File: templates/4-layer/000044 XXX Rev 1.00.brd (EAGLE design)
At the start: 259 x 228 mm, 22 parts, among them X1 PAD_TEST_GROUND_HOOK

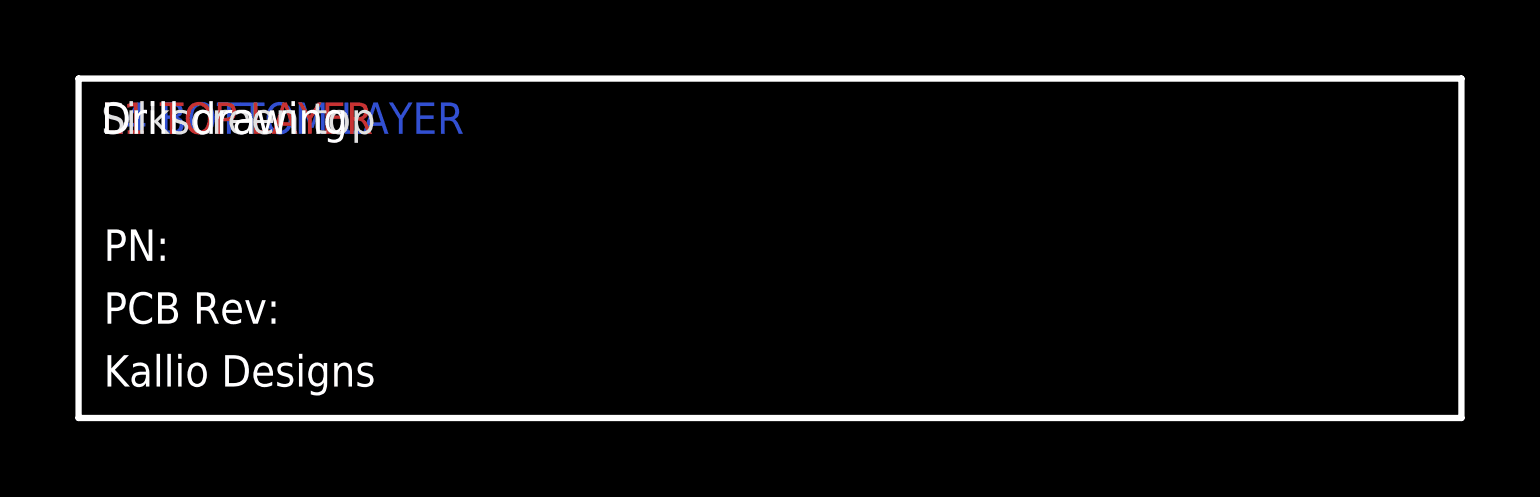
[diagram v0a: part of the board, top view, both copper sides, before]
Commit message: Template updates
For syncing with fusion
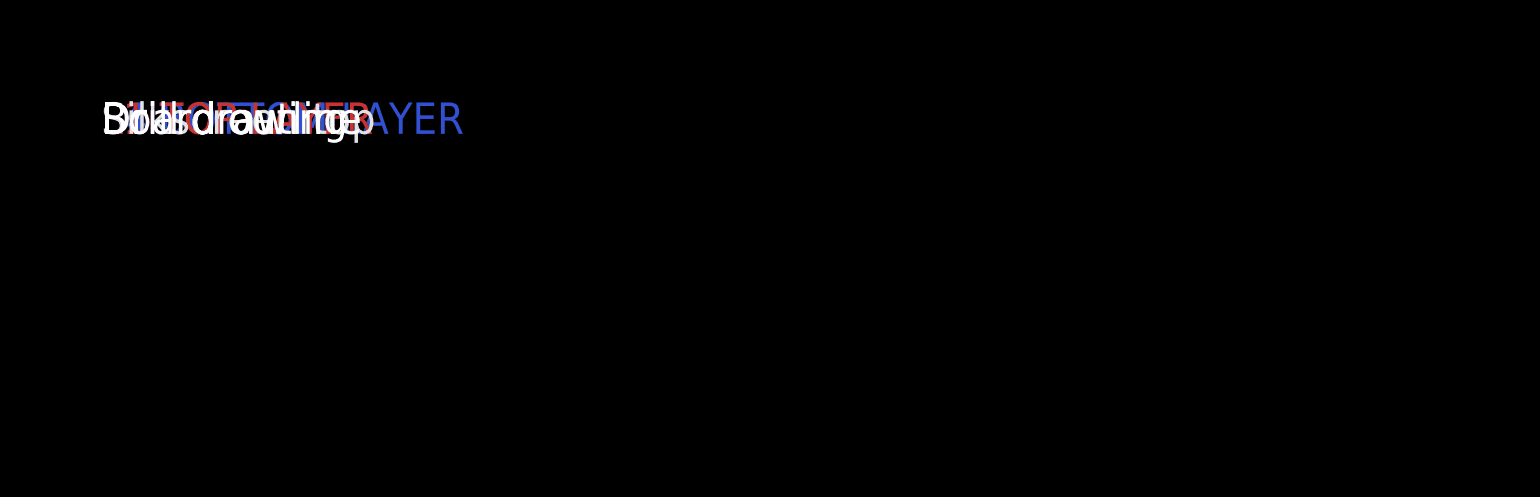
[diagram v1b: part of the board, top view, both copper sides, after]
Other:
- outline, holes or cut-outs redrawn
- board text added: "Board outline"
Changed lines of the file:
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@@
 <layer number="25" name="tNames" color="7" fill="1" visible="yes" active="yes"/>
 <layer number="26" name="bNames" color="11" fill="1" visible="yes" active="yes"/>
-<layer number="27" name="tValues" color="7" fill="1" visible="yes" active="yes"/>
+<layer number="27" name="tValues" color="7" fill="1" visible="no" active="yes"/>
 <layer number="28" name="bValues" color="7" fill="1" visible="no" active="yes"/>
 <layer number="29" name="tStop" color="7" fill="3" visible="yes" active="yes"/>
@@
 <text x="164" y="108" size="2.5" layer="46" font="vector" ratio="12" align="top-right">L3: Mid</text>
 <text x="133" y="27" size="2.5" layer="15" font="vector" ratio="12" align="top-left">L3 mid-layer</text>
-<text x="133.2" y="11.9" size="2.5" layer="20" font="vector" ratio="12" align="top-left">PCB Rev: </text>
+<text x="133.2" y="11.9" size="2.5" layer="48" font="vector" ratio="12" align="top-left">PCB Rev: </text>
 <text x="133" y="27" size="2.5" layer="16" font="vector" ratio="12" align="top-left">L4 BOTTOM LAYER</text>
 <text x="133" y="27" size="2.5" layer="21" font="vector" ratio="12" align="top-left">Silkscreen top</text>
@@
 <text x="133.2" y="23.9" size="2.5" layer="31" font="vector" ratio="12" align="top-left">Paste mask top</text>
 <text x="133.2" y="23.9" size="2.5" layer="32" font="vector" ratio="12" align="top-left">Paste mask bottom</text>
-<wire x1="131.2" y1="28.9" x2="241.2" y2="28.9" width="0.5" layer="20"/>
-<wire x1="241.2" y1="28.9" x2="241.2" y2="1.9" width="0.5" layer="20"/>
-<wire x1="241.2" y1="1.9" x2="131.2" y2="1.9" width="0.5" layer="20"/>
-<wire x1="131.2" y1="1.9" x2="131.2" y2="28.9" width="0.5" layer="20"/>
-<text x="133.2" y="6.9" size="2.5" layer="20" font="vector" ratio="12" align="top-left">&gt;OWNER</text>
-<text x="239.2" y="6.9" size="2.5" layer="20" font="vector" ratio="12" align="top-right">&gt;DATE</text>
-<text x="151.7" y="11.9" size="2.5" layer="20" font="vector" ratio="12" align="top-left">&gt;REVISION</text>
-<text x="133.2" y="16.9" size="2.5" layer="20" font="vector" ratio="12" align="top-left">PN: </text>
-<text x="140.2" y="16.9" size="2.5" layer="20" font="vector" ratio="12" align="top-left">&gt;PCB_PN</text>
+<wire x1="131.2" y1="28.9" x2="241.2" y2="28.9" width="0.5" layer="48"/>
+<wire x1="241.2" y1="28.9" x2="241.2" y2="1.9" width="0.5" layer="48"/>
+<wire x1="241.2" y1="1.9" x2="131.2" y2="1.9" width="0.5" layer="48"/>
+<wire x1="131.2" y1="1.9" x2="131.2" y2="28.9" width="0.5" layer="48"/>
+<text x="133.2" y="6.9" size="2.5" layer="48" font="vector" ratio="12" align="top-left">&gt;OWNER</text>
+<text x="239.2" y="6.9" size="2.5" layer="48" font="vector" ratio="12" align="top-right">&gt;DATE</text>
+<text x="151.7" y="11.9" size="2.5" layer="48" font="vector" ratio="12" align="top-left">&gt;REVISION</text>
+<text x="133.2" y="16.9" size="2.5" layer="48" font="vector" ratio="12" align="top-left">PN: </text>
+<text x="140.2" y="16.9" size="2.5" layer="48" font="vector" ratio="12" align="top-left">&gt;PCB_PN</text>
 <text x="133" y="27" size="2.5" layer="46" font="vector" ratio="12" align="top-left">Drill drawing</text>
 <text x="133" y="27" size="2.5" layer="1" font="vector" ratio="12" align="top-left">L1 TOP LAYER</text>
 <text x="133" y="27" size="2.5" layer="2" font="vector" ratio="12" align="top-left">L2 mid-layer</text>
+<text x="133" y="27" size="2.5" layer="20" font="vector" ratio="12" align="top-left">Board outline</text>
 </plain>
 <attributes>

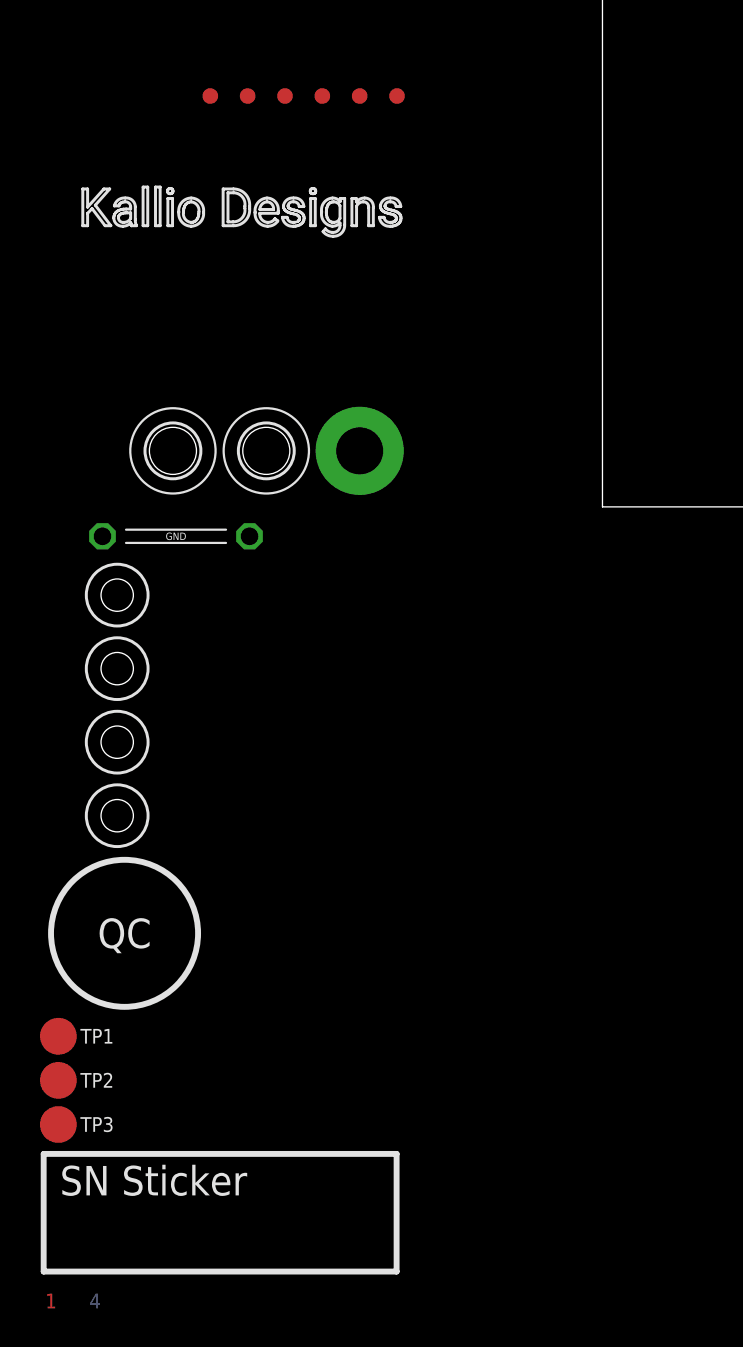
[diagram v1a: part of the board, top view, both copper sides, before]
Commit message: Changed templates to managed libraries
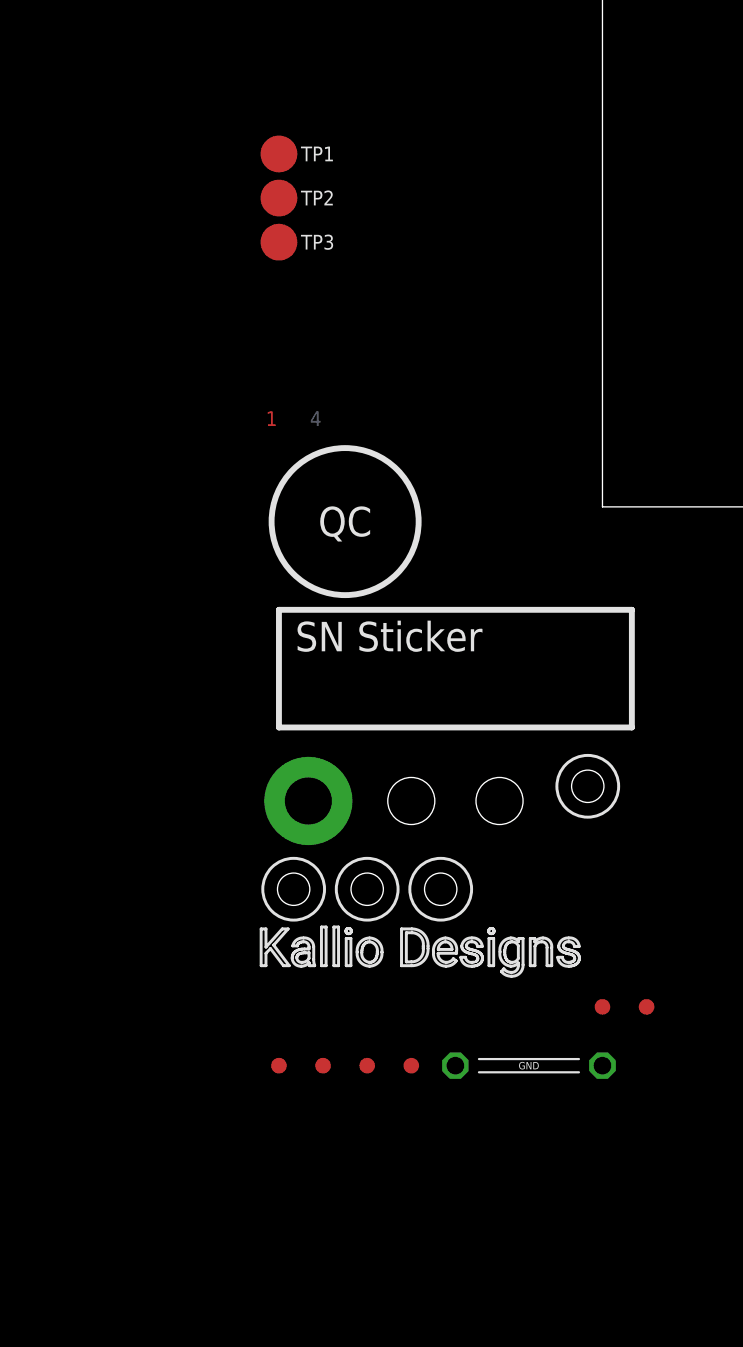
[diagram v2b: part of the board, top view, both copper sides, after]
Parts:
- MTG5, MTG6: value HOL_3.2/6.0_NP -> HOL_3.2/6.0_NP-NOSILK; device Custom_Eagle_KD:MTG_NP_M3_320X600 -> Custom_Eagle_KD:MTG_NP_M3_320X600_NOSILK
- moved FIDUCIAL6 67.3 mm to (-13.0, -38.0)
- moved FIDUCIAL5 66.4 mm to (-16.0, -38.0)
- moved FIDUCIAL3 66.0 mm to (-22.0, -38.0)
- moved FIDUCIAL4 66.0 mm to (-19.0, -38.0)
- moved FIDUCIAL2 64.9 mm to (3.00, -34.0)
- moved FIDUCIAL1 63.5 mm to (0.00, -34.0)
- moved LAYER1 61.8 mm to (-21.0, 6.00)
- moved TP1 61.8 mm to (-22.0, 24.0)
- moved TP2 61.8 mm to (-22.0, 21.0)
- moved TP3 61.8 mm to (-22.0, 18.0)
- moved LOGO3 59.4 mm to (-12.0, -34.0)
- moved LOGO2 51.8 mm to (-12.0, -30.0)
- moved X1 43.3 mm to (-5.00, -38.0)
- moved ART2 40.3 mm to (-22.0, -15.0)
- moved MTG1 34.5 mm to (-1.00, -19.0)
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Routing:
- added copper zone on layer 15, net +3V1
- added copper zone on layer 2, net GND1
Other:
- board text added: "2"
- board text added: "3"
